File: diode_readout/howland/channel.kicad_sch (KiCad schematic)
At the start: 10 parts, among them U1 MCP3421A0T-ECH

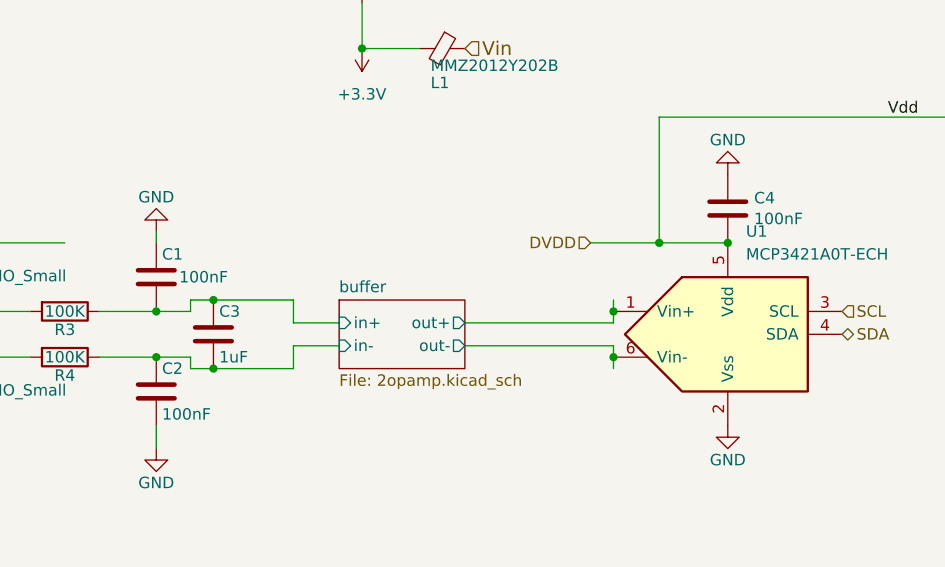
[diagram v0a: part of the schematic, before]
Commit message: add sq_lockin_v8 and tweaks to howland diode_readout
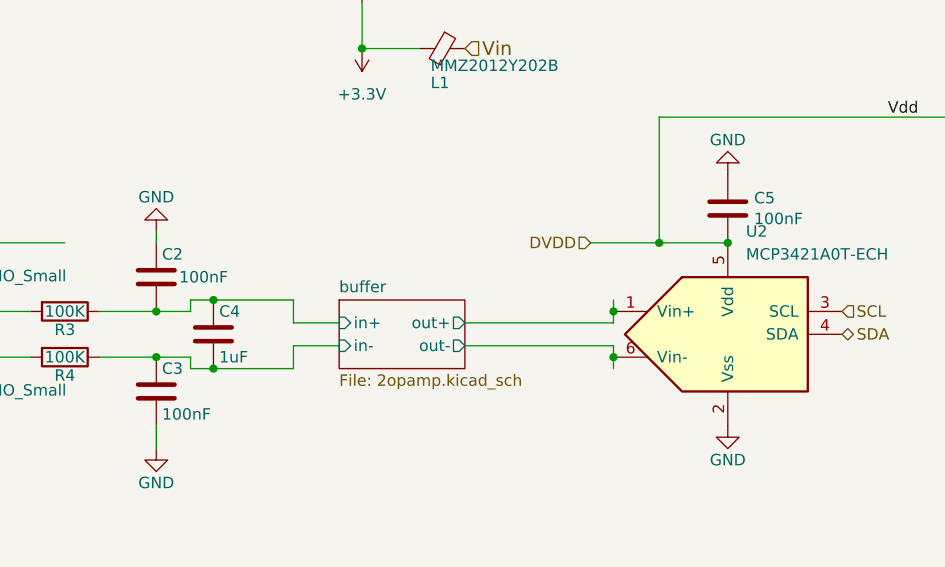
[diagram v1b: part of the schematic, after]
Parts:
- renumbered C1 to C2, C2 to C3, C3 to C4, C4 to C5, U1 to U2
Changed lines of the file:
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@@
   (symbol (lib_id "0JLC-6:100nF") (at 184.15 77.47 180) (unit 1)
     (in_bom yes) (on_board yes)
-    (property "Reference" "C4" (id 0) (at 187.071 76.3016 0)
+    (property "Reference" "C5" (id 0) (at 187.071 76.3016 0)
       (effects (font (size 1.27 1.27)) (justify right))
     )
@@
   (symbol (lib_id "Device:C") (at 120.65 97.79 0) (unit 1)
     (in_bom yes) (on_board yes)
-    (property "Reference" "C2" (id 0) (at 121.285 95.25 0)
+    (property "Reference" "C3" (id 0) (at 121.285 95.25 0)
       (effects (font (size 1.27 1.27)) (justify left))
     )
@@
   (symbol (lib_id "Device:C") (at 120.65 85.09 0) (unit 1)
     (in_bom yes) (on_board yes)
-    (property "Reference" "C1" (id 0) (at 121.285 82.55 0)
+    (property "Reference" "C2" (id 0) (at 121.285 82.55 0)
       (effects (font (size 1.27 1.27)) (justify left))
     )
@@
   (symbol (lib_id "Device:C") (at 127 91.44 0) (unit 1)
     (in_bom yes) (on_board yes)
-    (property "Reference" "C3" (id 0) (at 127.635 88.9 0)
+    (property "Reference" "C4" (id 0) (at 127.635 88.9 0)
       (effects (font (size 1.27 1.27)) (justify left))
     )
@@
   (symbol (lib_id "power:GND") (at 120.65 104.14 0) (unit 1)
     (in_bom yes) (on_board yes)
-    (property "Reference" "#PWR05" (id 0) (at 120.65 110.49 0)
+    (property "Reference" "#PWR06" (id 0) (at 120.65 110.49 0)
       (effects (font (size 1.27 1.27)) hide)
     )
@@
   (symbol (lib_id "power:GND") (at 120.65 80.01 180) (unit 1)
     (in_bom yes) (on_board yes)
-    (property "Reference" "#PWR04" (id 0) (at 120.65 73.66 0)
+    (property "Reference" "#PWR05" (id 0) (at 120.65 73.66 0)
       (effects (font (size 1.27 1.27)) hide)
     )
@@
   (symbol (lib_id "power:GND") (at 184.15 73.66 180) (unit 1)
     (in_bom yes) (on_board yes)
-    (property "Reference" "#PWR07" (id 0) (at 184.15 67.31 0)
+    (property "Reference" "#PWR08" (id 0) (at 184.15 67.31 0)
       (effects (font (size 1.27 1.27)) hide)
     )
@@
   (symbol (lib_id "power:GND") (at 184.15 101.6 0) (unit 1)
     (in_bom yes) (on_board yes)
-    (property "Reference" "#PWR08" (id 0) (at 184.15 107.95 0)
+    (property "Reference" "#PWR09" (id 0) (at 184.15 107.95 0)
       (effects (font (size 1.27 1.27)) hide)
     )
@@
   (symbol (lib_id "power:+3.3V") (at 143.51 59.69 180) (unit 1)
     (in_bom yes) (on_board yes) (fields_autoplaced)
-    (property "Reference" "#PWR06" (id 0) (at 143.51 55.88 0)
+    (property "Reference" "#PWR07" (id 0) (at 143.51 55.88 0)
       (effects (font (size 1.27 1.27)) hide)
     )
@@
   (symbol (lib_id "Analog_ADC:MCP3421A0T-ECH") (at 184.15 91.44 0) (unit 1)
     (in_bom yes) (on_board yes) (fields_autoplaced)
-    (property "Reference" "U1" (id 0) (at 186.1694 80.01 0)
-      (effects (font (size 1.27 1.27)) (justify left))
-    )
+    (property "Reference" "U2" (id 0) (at 186.1694 80.01 0)
+      (effects (font (size 1.27 1.27)) (justify left))
+    )

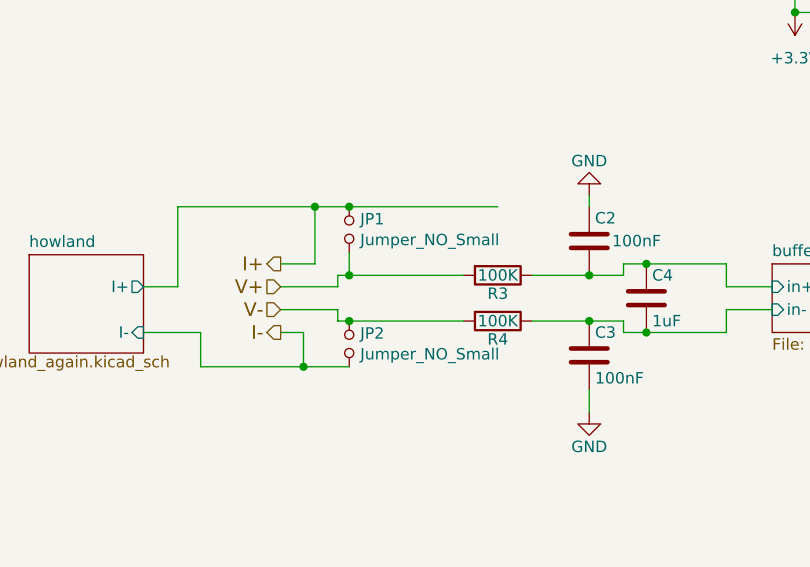
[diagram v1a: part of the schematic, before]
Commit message: Commit changes to howland current source diode readout: 1.  Add 1Mohm shorts bettern V+ and I+  as well as V- and I- to mimic      this will mimic the two wire readout behaviour when the diode gets      disconnected. 2.  Add FRAM chip, 512kbits or 64kBytes of memory
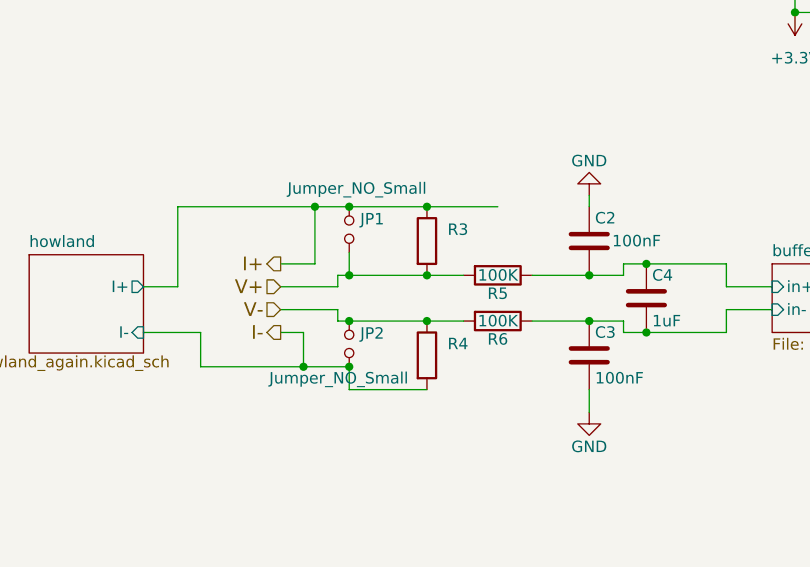
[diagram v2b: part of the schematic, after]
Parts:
- added R3, R4: (no value), symbol 0JLC-6:1M_0.1%
- renumbered R3 to R5, R4 to R6
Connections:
- net I+: now also R3.1
- net I-: now also R4.2
- net V+: now also R3.2
- net V-: now also R4.1
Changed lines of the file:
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@@
   (junction (at 184.15 81.28) (diameter 0) (color 0 0 0 0)
   )
+  (junction (at 102.616 88.9) (diameter 0) (color 0 0 0 0)
+  )
   (junction (at 171.45 93.98) (diameter 0) (color 0 0 0 0)
   )
@@
   (junction (at 176.53 81.28) (diameter 0) (color 0 0 0 0)
   )
+  (junction (at 102.616 93.98) (diameter 0) (color 0 0 0 0)
+  )
   (junction (at 90.17 81.28) (diameter 0) (color 0 0 0 0)
   )
@@
   (junction (at 120.65 93.98) (diameter 0) (color 0 0 0 0)
   )
+  (junction (at 102.616 81.28) (diameter 0) (color 0 0 0 0)
+  )
   (junction (at 127 87.63) (diameter 0) (color 0 0 0 0)
   )
@@
   (junction (at 93.98 88.9) (diameter 0) (color 0 0 0 0)
   )
+  (junction (at 93.98 99.06) (diameter 0) (color 0 0 0 0)
+  )
   (junction (at 143.51 59.69) (diameter 0) (color 0 0 0 0)
   )
@@
     (stroke (width 0) (type default) (color 0 0 0 0))
   )
+  (wire (pts (xy 102.616 101.6) (xy 93.98 101.6))
+    (stroke (width 0) (type default) (color 0 0 0 0))
+  )
   (wire (pts (xy 135.89 92.71) (xy 140.97 92.71))
     (stroke (width 0) (type default) (color 0 0 0 0))
@@
     (stroke (width 0) (type default) (color 0 0 0 0))
   )
-  (wire (pts (xy 106.68 93.98) (xy 93.98 93.98))
+  (wire (pts (xy 106.68 93.98) (xy 102.616 93.98))
     (stroke (width 0) (type default) (color 0 0 0 0))
   )
@@
     (stroke (width 0) (type default) (color 0 0 0 0))
   )
+  (wire (pts (xy 102.616 93.98) (xy 93.98 93.98))
+    (stroke (width 0) (type default) (color 0 0 0 0))
+  )
   (wire (pts (xy 90.17 81.28) (xy 93.98 81.28))
     (stroke (width 0) (type default) (color 0 0 0 0))
@@
     (stroke (width 0) (type default) (color 0 0 0 0))
   )
-  (wire (pts (xy 93.98 81.28) (xy 110.49 81.28))
-    (stroke (width 0) (type default) (color 0 0 0 0))
-  )
   (wire (pts (xy 86.36 95.25) (xy 88.9 95.25))
     (stroke (width 0) (type default) (color 0 0 0 0))
@@
     (stroke (width 0) (type default) (color 0 0 0 0))
   )
+  (wire (pts (xy 102.616 88.9) (xy 106.68 88.9))
+    (stroke (width 0) (type default) (color 0 0 0 0))
+  )
   (wire (pts (xy 135.89 95.25) (xy 135.89 92.71))
     (stroke (width 0) (type default) (color 0 0 0 0))
@@
     (stroke (width 0) (type default) (color 0 0 0 0))
   )
-  (wire (pts (xy 106.68 88.9) (xy 93.98 88.9))
+  (wire (pts (xy 93.98 88.9) (xy 102.616 88.9))
     (stroke (width 0) (type default) (color 0 0 0 0))
   )
@@
     (stroke (width 0) (type default) (color 0 0 0 0))
   )
+  (wire (pts (xy 93.98 101.6) (xy 93.98 99.06))
+    (stroke (width 0) (type default) (color 0 0 0 0))
+  )
   (wire (pts (xy 143.51 54.61) (xy 143.51 59.69))
     (stroke (width 0) (type default) (color 0 0 0 0))
   )
+  (wire (pts (xy 102.616 81.28) (xy 110.49 81.28))
+    (stroke (width 0) (type default) (color 0 0 0 0))
+  )
   (wire (pts (xy 93.98 93.98) (xy 92.71 93.98))
     (stroke (width 0) (type default) (color 0 0 0 0))
   )
   (wire (pts (xy 71.12 90.17) (xy 74.93 90.17))
+    (stroke (width 0) (type default) (color 0 0 0 0))
+  )
+  (wire (pts (xy 93.98 81.28) (xy 102.616 81.28))
     (stroke (width 0) (type default) (color 0 0 0 0))
   )
@@
   (symbol (lib_id "Device:R") (at 110.49 88.9 270) (unit 1)
     (in_bom yes) (on_board yes)
-    (property "Reference" "R3" (id 0) (at 110.49 90.932 90))
+    (property "Reference" "R5" (id 0) (at 110.49 90.932 90))
     (property "Value" "100K" (id 1) (at 110.49 88.9 90))
     (property "Footprint" "Resistor_SMD:R_0402_1005Metric" (id 2) (at 110.49 87.122 90)
@@
   (symbol (lib_id "Device:R") (at 110.49 93.98 270) (unit 1)
     (in_bom yes) (on_board yes)
-    (property "Reference" "R4" (id 0) (at 110.49 96.012 90))
+    (property "Reference" "R6" (id 0) (at 110.49 96.012 90))
     (property "Value" "100K" (id 1) (at 110.49 93.98 90))
     (property "Footprint" "Resistor_SMD:R_0402_1005Metric" (id 2) (at 110.49 92.202 90)
@@
       (effects (font (size 1.27 1.27)) (justify left))
     )
-    (property "Value" "Jumper_NO_Small" (id 1) (at 95.1992 84.963 90)
+    (property "Value" "Jumper_NO_Small" (id 1) (at 87.122 79.248 90)
       (effects (font (size 1.27 1.27)) (justify left))
     )
@@
       (effects (font (size 1.27 1.27)) (justify left))
     )
-    (property "Value" "Jumper_NO_Small" (id 1) (at 95.1992 97.663 90)
+    (property "Value" "Jumper_NO_Small" (id 1) (at 85.09 100.33 90)
       (effects (font (size 1.27 1.27)) (justify left))
     )
@@
     )
     (property "Datasheet" "~" (id 3) (at 93.98 96.52 0)
+      (effects (font (size 1.27 1.27)) hide)
+    )
+    (pin "1")
+    (pin "2")
+  )
+  (symbol (lib_id "0JLC-6:1M_0.1%") (at 102.616 97.79 0) (unit 1)
+    (in_bom yes) (on_board yes) (fields_autoplaced)
+    (property "Reference" "R4" (id 0) (at 104.902 96.5199 0)
+      (effects (font (size 1.27 1.27)) (justify left))
+    )
+    (property "Value" "" (id 1) (at 104.902 99.0599 0)
+      (effects (font (size 1.27 1.27)) (justify left))
+    )
+    (property "Footprint" "" (id 2) (at 100.838 97.79 90)
+      (effects (font (size 1.27 1.27)) hide)
+    )
+    (property "Datasheet" "~" (id 3) (at 102.616 97.79 0)
+      (effects (font (size 1.27 1.27)) hide)
+    )
+    (property "LCSC" "C138033" (id 4) (at 102.616 97.79 0)
+      (effects (font (size 1.27 1.27)) hide)
+    )
+    (property "MPN" "RC0402FR-071ML" (id 5) (at 102.616 97.79 0)
       (effects (font (size 1.27 1.27)) hide)
     )
@@
     (pin "1")
   )
+  (symbol (lib_id "0JLC-6:1M_0.1%") (at 102.616 85.09 0) (unit 1)
+    (in_bom yes) (on_board yes) (fields_autoplaced)
+    (property "Reference" "R3" (id 0) (at 104.902 83.8199 0)
+      (effects (font (size 1.27 1.27)) (justify left))
+    )
+    (property "Value" "" (id 1) (at 104.902 86.3599 0)
+      (effects (font (size 1.27 1.27)) (justify left))
+    )
+    (property "Footprint" "" (id 2) (at 100.838 85.09 90)
+      (effects (font (size 1.27 1.27)) hide)
+    )
+    (property "Datasheet" "~" (id 3) (at 102.616 85.09 0)
+      (effects (font (size 1.27 1.27)) hide)
+    )
+    (property "LCSC" "C138033" (id 4) (at 102.616 85.09 0)
+      (effects (font (size 1.27 1.27)) hide)
+    )
+    (property "MPN" "RC0402FR-071ML" (id 5) (at 102.616 85.09 0)
+      (effects (font (size 1.27 1.27)) hide)
+    )
+    (pin "1")
+    (pin "2")
+  )
   (symbol (lib_id "Analog_ADC:MCP3421A0T-ECH") (at 184.15 91.44 0) (unit 1)

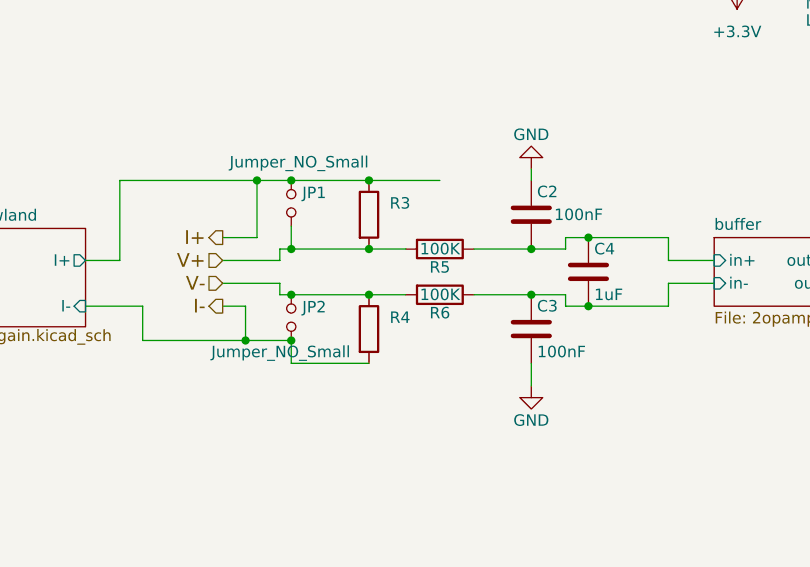
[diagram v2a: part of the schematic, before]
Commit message: tweak 10K resistors because of parts shortages
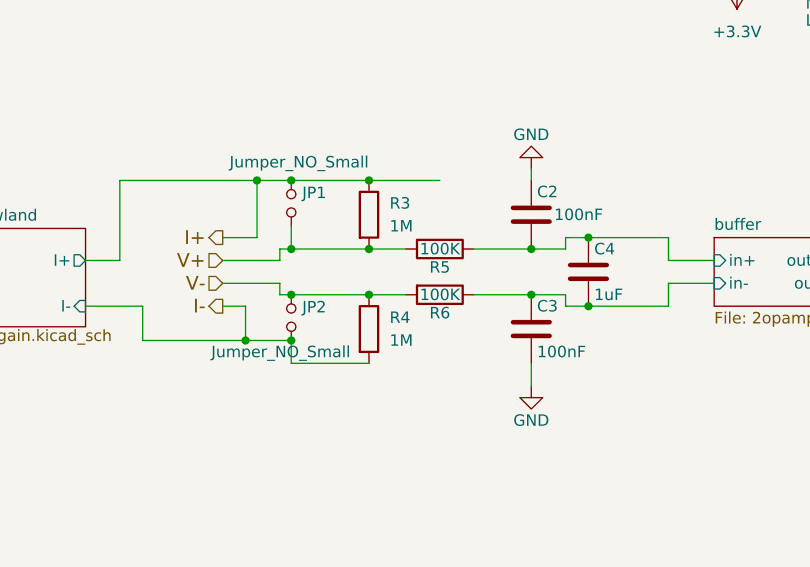
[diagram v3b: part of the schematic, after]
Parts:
- R3, R4: value (none) -> 1M; footprint (none) -> Resistor_SMD:R_0402_1005Metric
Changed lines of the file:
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@@
       (effects (font (size 1.27 1.27)) (justify left))
     )
-    (property "Value" "" (id 1) (at 104.902 99.0599 0)
+    (property "Value" "1M" (id 1) (at 104.902 99.0599 0)
       (effects (font (size 1.27 1.27)) (justify left))
     )
-    (property "Footprint" "" (id 2) (at 100.838 97.79 90)
+    (property "Footprint" "Resistor_SMD:R_0402_1005Metric" (id 2) (at 100.838 97.79 90)
       (effects (font (size 1.27 1.27)) hide)
     )
@@
       (effects (font (size 1.27 1.27)) (justify left))
     )
-    (property "Value" "" (id 1) (at 104.902 86.3599 0)
+    (property "Value" "1M" (id 1) (at 104.902 86.3599 0)
       (effects (font (size 1.27 1.27)) (justify left))
     )
-    (property "Footprint" "" (id 2) (at 100.838 85.09 90)
+    (property "Footprint" "Resistor_SMD:R_0402_1005Metric" (id 2) (at 100.838 85.09 90)
       (effects (font (size 1.27 1.27)) hide)
     )
